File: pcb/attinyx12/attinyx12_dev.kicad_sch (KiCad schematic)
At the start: 20 parts, among them J2 Conn_01x03, J3 Conn_01x06, J4 Conn_01x06, J6 USB_B_Micro, SW1 SW_Push, U1 ATtiny212-SS, U3 CH342K

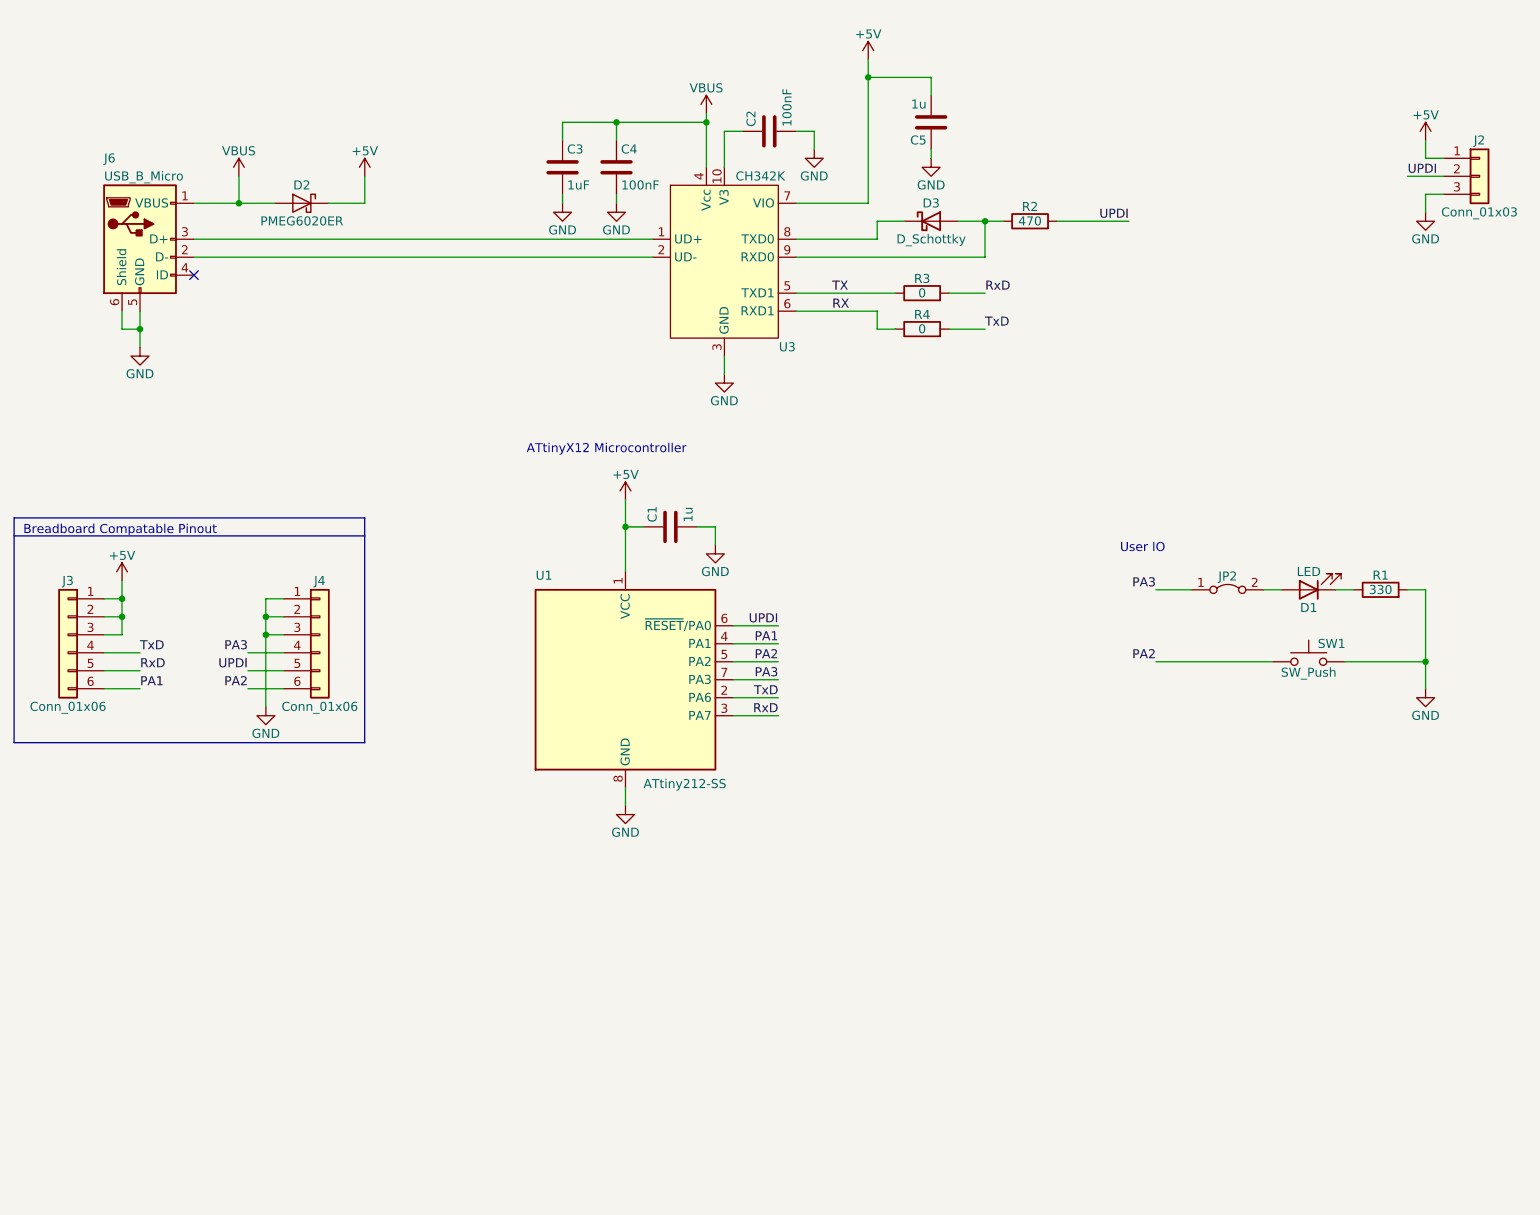
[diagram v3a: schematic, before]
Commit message: Update attinyx12_dev.kicad_sch
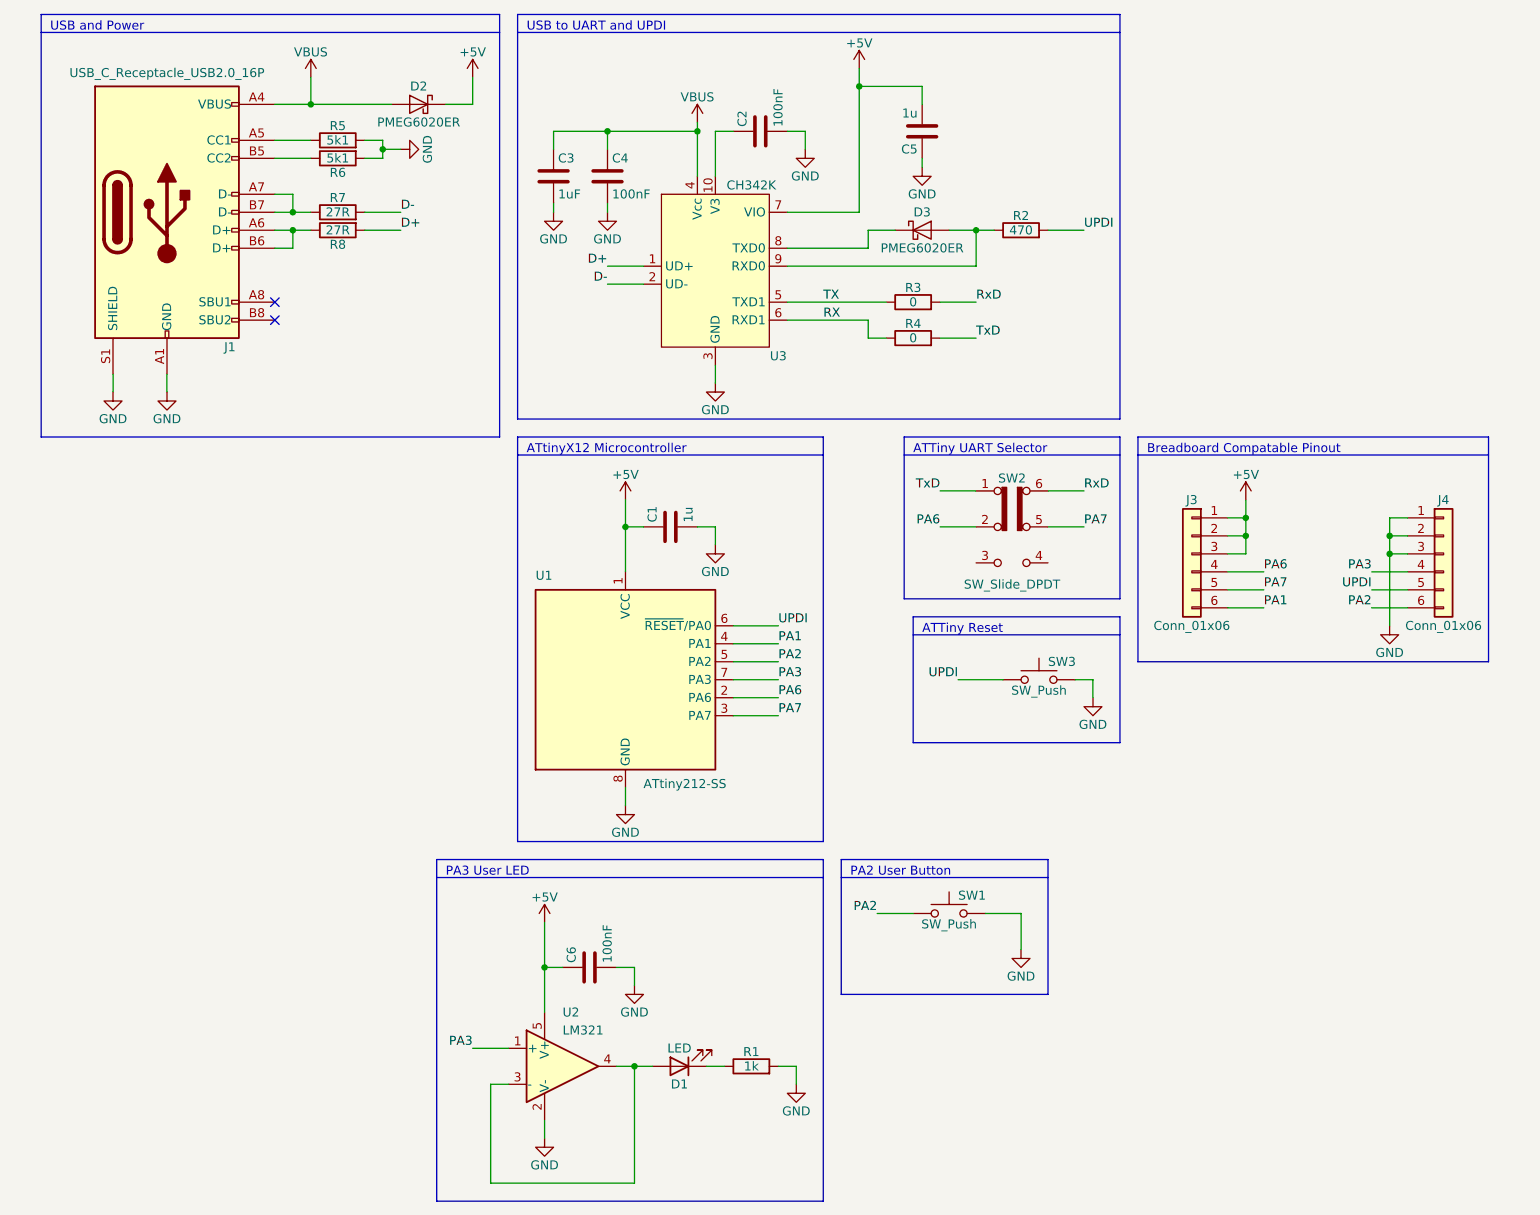
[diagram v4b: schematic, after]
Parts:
- removed D3: D_Schottky, symbol Device:D_Schottky
- removed J2: Conn_01x03, Connector_PinHeader_2.54mm:PinHeader_1x03_P2.54mm_Vertical, symbol Connector_Generic:Conn_01x03
- removed J6: USB_B_Micro, symbol Connector:USB_B_Micro
- removed JP2: Jumper_2_Bridged, Connector_PinHeader_2.54mm:PinHeader_1x02_P2.54mm_Vertical, symbol Jumper:Jumper_2_Bridged
- added C6: 100nF, Capacitor_SMD:C_0603_1608Metric, symbol Device:C
- added D3: PMEG6020ER, Diode_SMD:Nexperia_CFP3_SOD-123W, symbol Diode:PMEG6020ER
- added J1: USB_C_Receptacle_USB2.0_16P, Connector_USB:USB_C_Receptacle_G-Switch_GT-USB-7010ASV, symbol Connector:USB_C_Receptacle_USB2.0_16P
- added R5, R6: 5k1, Resistor_SMD:R_0603_1608Metric, symbol Device:R
- added R7, R8: 27R, Resistor_SMD:R_0603_1608Metric, symbol Device:R
- added SW2: SW_Slide_DPDT, symbol Switch:SW_Slide_DPDT
- added SW3: SW_Push, Button_Switch_SMD:SW_SPST_CK_RS282G05A3, symbol Switch:SW_Push
- added U2: LM321, Package_TO_SOT_SMD:SOT-23-5, symbol Amplifier_Operational:LM321
- C1, C5: footprint Capacitor_SMD:C_1210_3225Metric_Pad1.33x2.70mm_HandSolder -> Capacitor_SMD:C_0603_1608Metric
- C2, C3, C4: footprint (none) -> Capacitor_SMD:C_0603_1608Metric
- D1: footprint LED_THT:LED_D3.0mm -> LED_SMD:LED_0603_1608Metric
- J3, J4: footprint (none) -> Connector_PinHeader_2.54mm:PinHeader_1x06_P2.54mm_Vertical
- R1: value 330 -> 1k; footprint Resistor_THT:R_Axial_DIN0207_L6.3mm_D2.5mm_P10.16mm_Horizontal -> Resistor_SMD:R_0603_1608Metric
- R2, R3, R4: footprint (none) -> Resistor_SMD:R_0805_2012Metric
- SW1: footprint (none) -> Button_Switch_SMD:SW_SPST_CK_RS282G05A3
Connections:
- net +5V: now also C6.1, U2.5 (V+)
- net GND: now also C6.2, J1.A1 (GND), J1.A12 (GND), J1.B1 (GND), J1.B12 (GND), J1.S1 (SHIELD), R5.2, R6.2, SW3.2, U2.2 (V-)
- net PA3: now also U2.1 (+)
- net RxD: now also SW2.6 (C); no longer J3.5 (Pin_5), U1.3 (PA7)
- net TxD: now also SW2.1 (A); no longer J3.4 (Pin_4), U1.2 (PA6)
- net UPDI: now also SW3.1
- net VBUS: now also J1.A4 (VBUS), J1.A9 (VBUS), J1.B4 (VBUS), J1.B9 (VBUS)
- net D+: now reaches U3.1 (UD+)
- net D+: now also R8.2
- net D-: now reaches U3.2 (UD-)
- net D-: now also R7.2
- net at U3.8 (TXD0): now also D3.1 (K)
- net at R2.1, U3.9 (RXD0): now also D3.2 (A)
- net at D1.2 (A): now also U2.3 (-), U2.4
- new net: J1.A6 (D+), J1.B6 (D+), R8.1
- new net: J1.A7 (D-), J1.B7 (D-), R7.1
- new net: J1.A5 (CC1), R5.1
- new net: J1.B5 (CC2), R6.1
- new net PA6: J3.4 (Pin_4), SW2.2 (B), U1.2 (PA6)
- new net PA7: J3.5 (Pin_5), SW2.5 (B), U1.3 (PA7)
- no-connect marks 1 -> 2
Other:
- note added: "ATTiny Reset"
- note added: "ATTiny UART Selector"
- note added: "PA2 User Button"
- note added: "PA3 User LED"
- note added: "USB and Power"
- note added: "USB to UART and UPDI"
- note removed: "User IO"
- moved on the sheet: C2, C3, C4, C5, D1, D2, J3, J4, R1, R2, R3, R4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

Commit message: schema done
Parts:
- SW2: footprint (none) -> pl_DPDT:MST22D18G_125
- renumbered C3 to C1, C6 to C2, C4 to C3, C1 to C4, C2 to C5, C5 to C6, D2 to D1, D1 to D2, J3 to J2, J4 to J3, R5 to R1, R6 to R2, R7 to R3, R8 to R4, R1 to R5, R3 to R6, R4 to R7, R2 to R8, U2 to U1, U1 to U2
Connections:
- no-connect marks 2 -> 4
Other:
- moved on the sheet: D1, J1, R1, R2, R3, R4

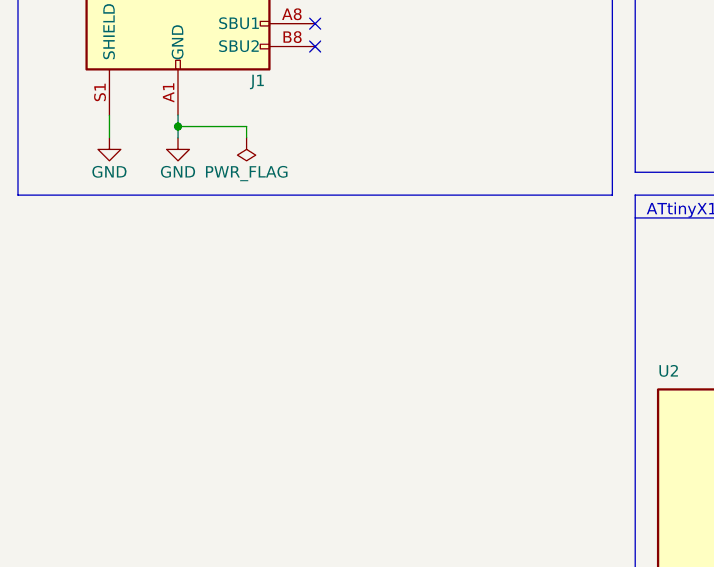
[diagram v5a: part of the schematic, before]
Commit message: add mounting holes
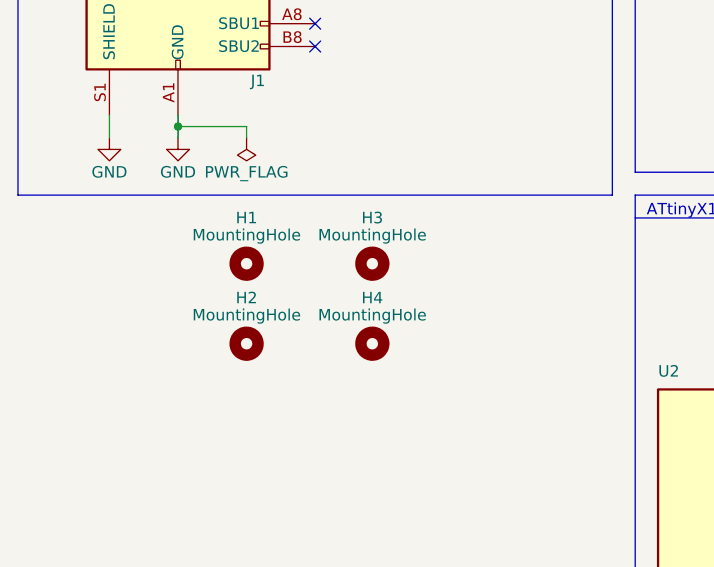
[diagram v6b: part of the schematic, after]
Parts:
- added H1, H2, H3, H4: MountingHole, MountingHole:MountingHole_3.2mm_M3, symbol Mechanical:MountingHole

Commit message: reduce mounting holes to 2.5mm
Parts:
- H1, H2, H3, H4: footprint MountingHole:MountingHole_3.2mm_M3 -> MountingHole:MountingHole_2.7mm_M2.5
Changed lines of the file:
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@@
 			)
 		)
-		(property "Footprint" "MountingHole:MountingHole_3.2mm_M3"
+		(property "Footprint" "MountingHole:MountingHole_2.7mm_M2.5"
 			(at 69.85 81.28 0)
 			(effects
@@
 			)
 		)
-		(property "Footprint" "MountingHole:MountingHole_3.2mm_M3"
+		(property "Footprint" "MountingHole:MountingHole_2.7mm_M2.5"
 			(at 83.82 90.17 0)
 			(effects
@@
 			)
 		)
-		(property "Footprint" "MountingHole:MountingHole_3.2mm_M3"
+		(property "Footprint" "MountingHole:MountingHole_2.7mm_M2.5"
 			(at 69.85 90.17 0)
 			(effects
@@
 			)
 		)
-		(property "Footprint" "MountingHole:MountingHole_3.2mm_M3"
+		(property "Footprint" "MountingHole:MountingHole_2.7mm_M2.5"
 			(at 83.82 81.28 0)
 			(effects

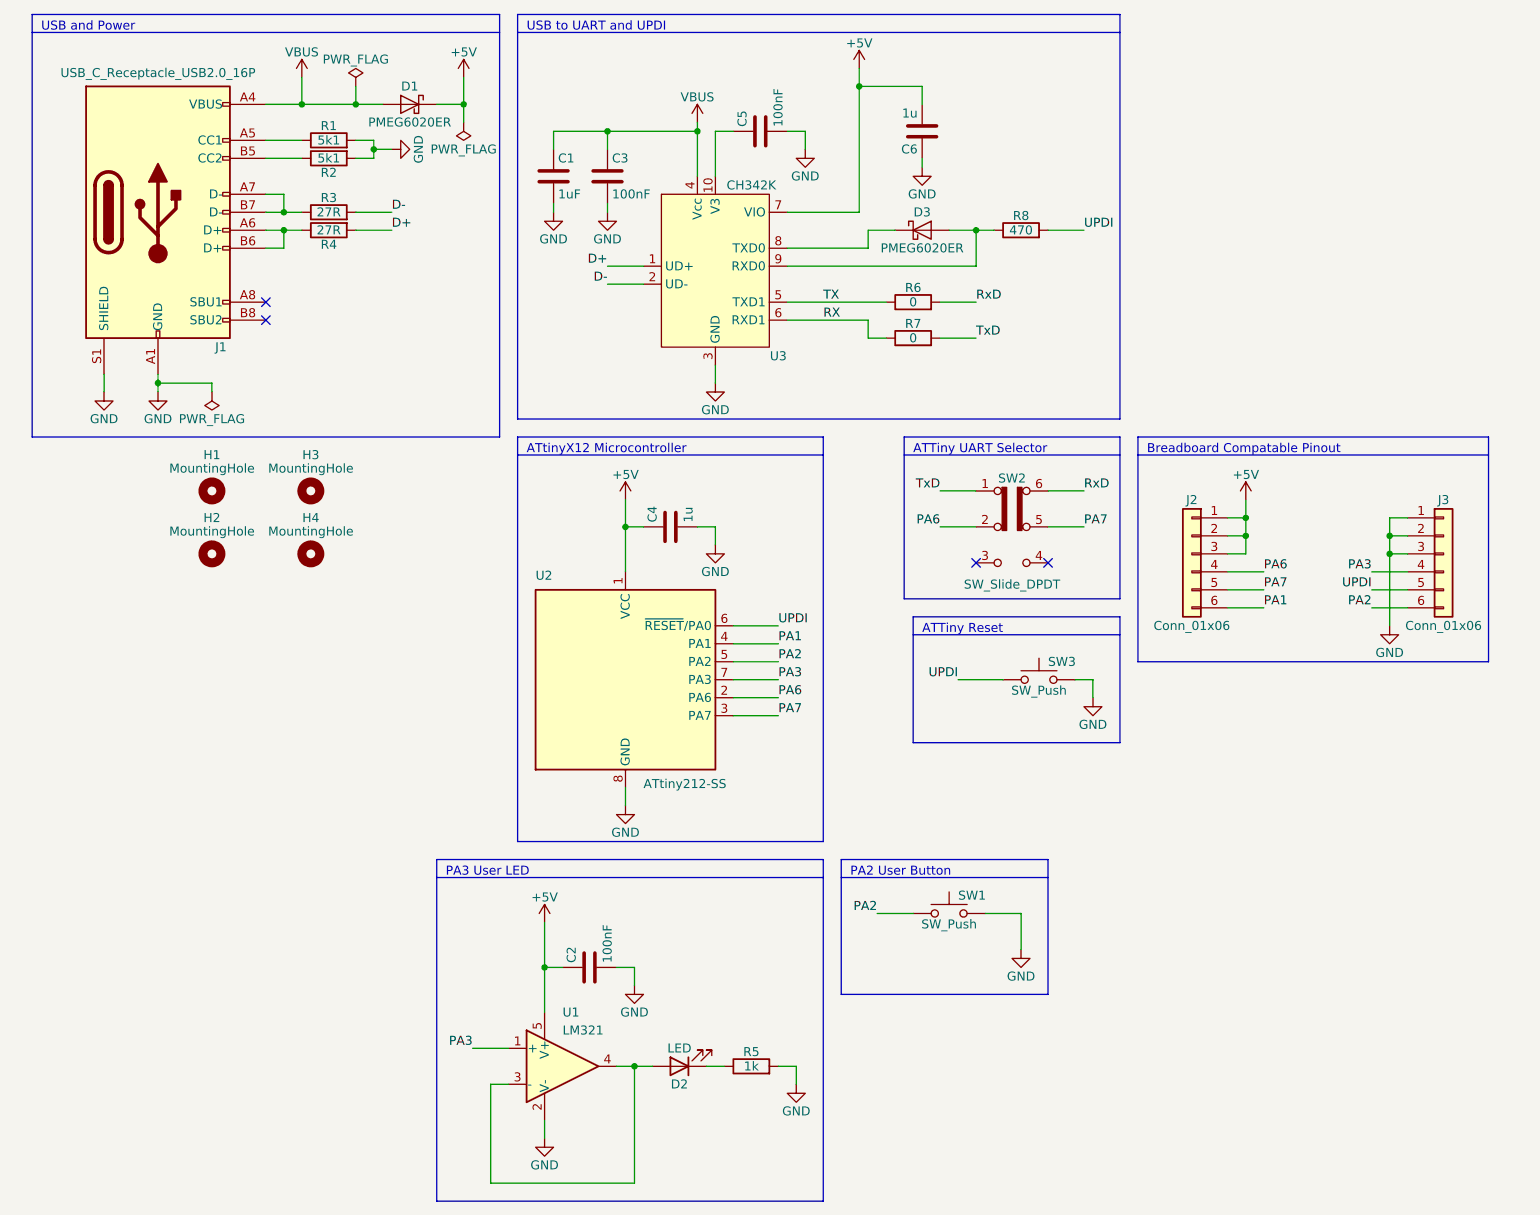
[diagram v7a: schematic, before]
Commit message: replace switch with jumpers, remove buttons
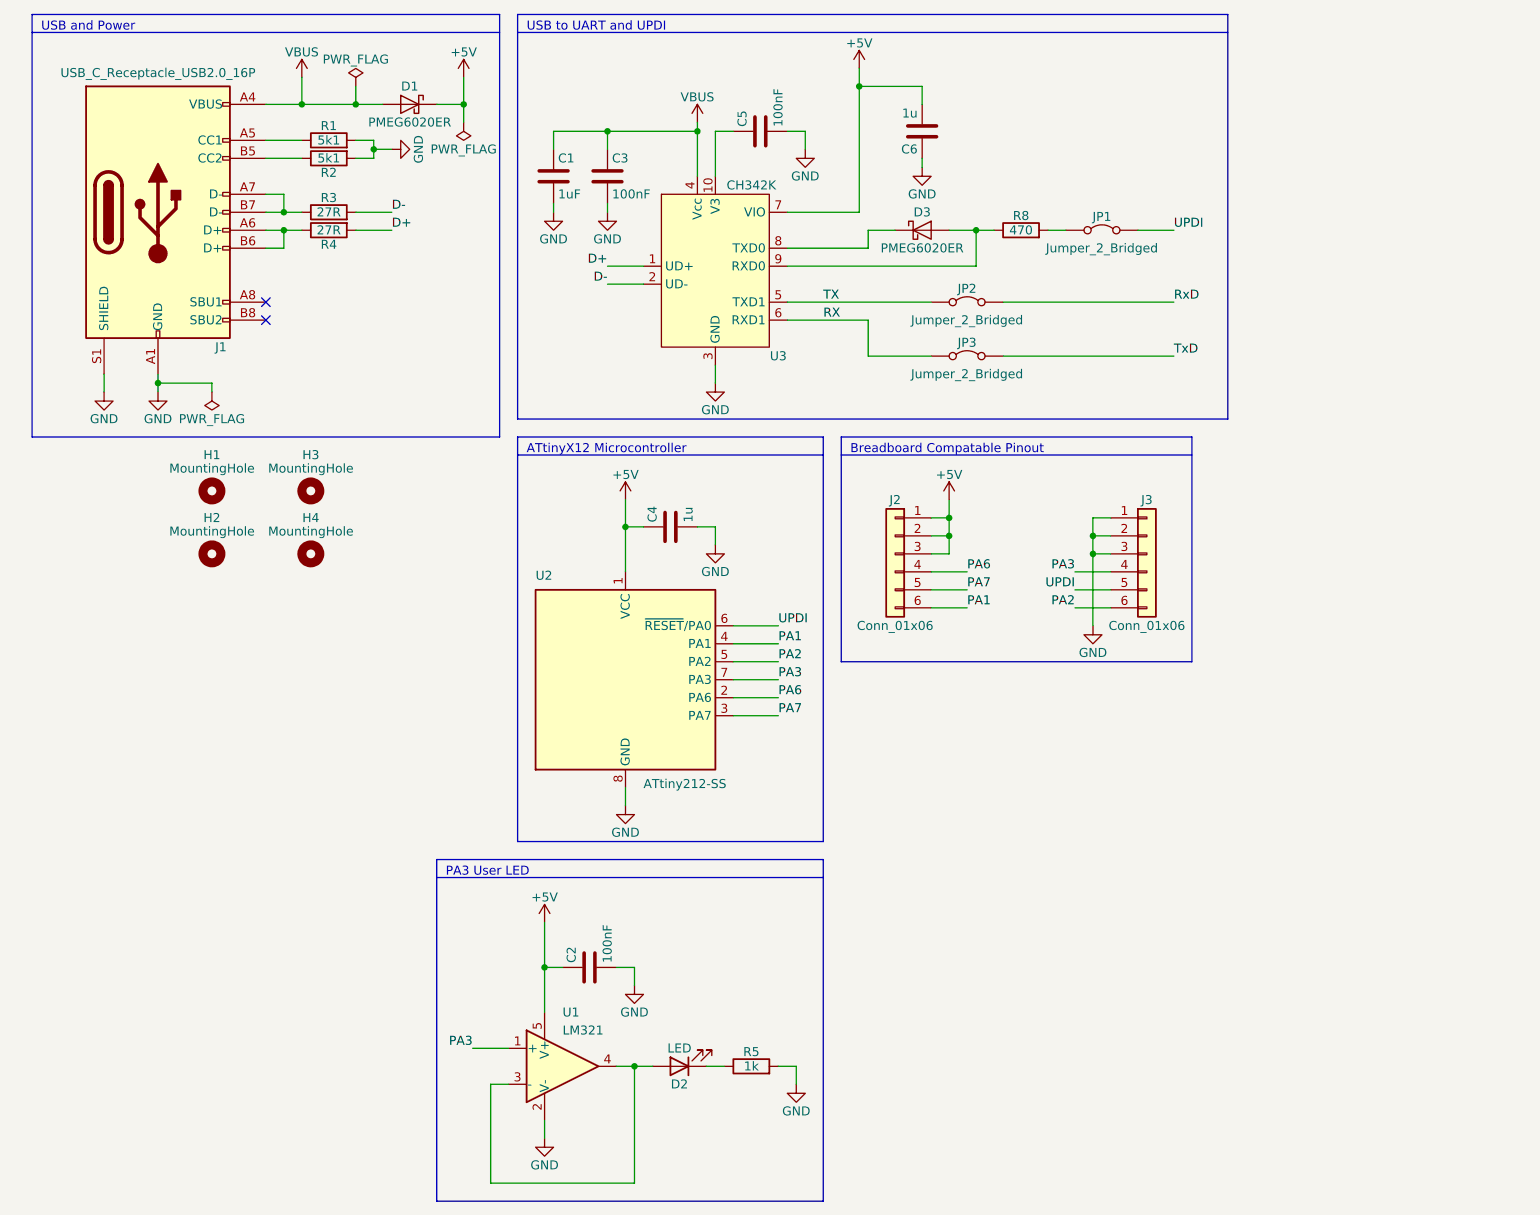
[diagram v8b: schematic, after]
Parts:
- removed R6, R7: 0, Resistor_SMD:R_0805_2012Metric, symbol Device:R
- removed SW1, SW3: SW_Push, Button_Switch_SMD:SW_SPST_CK_RS282G05A3, symbol Switch:SW_Push
- removed SW2: SW_Slide_DPDT, pl_DPDT:MST22D18G_125, symbol Switch:SW_Slide_DPDT
- added JP1, JP2, JP3: Jumper_2_Bridged, Jumper:SolderJumper-2_P1.3mm_Bridged_RoundedPad1.0x1.5mm, symbol Jumper:Jumper_2_Bridged
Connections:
- net RX: now also JP3.1 (A)
- net RxD: now also JP2.2 (B)
- net TX: now also JP2.1 (A)
- net TxD: now also JP3.2 (B)
- net UPDI: now also JP1.2 (B); no longer R8.2
- new net: JP1.1 (A), R8.2
- no-connect marks 4 -> 2
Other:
- note removed: "ATTiny Reset"
- note removed: "ATTiny UART Selector"
- note removed: "PA2 User Button"
- moved on the sheet: J2, J3
